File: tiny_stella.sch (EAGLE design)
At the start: 73 parts, among them SW1 RGT_DIFFICULTY, SW2 LFT_DIFFICULTY, SW3 ON/OFF, T1 2N3904, T2 PN3906, T3 PN3906, X1 SSW-112-02-G-Q

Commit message: labeled everything and started laying traces
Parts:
- S3, S4: device SparkFun-Switches:MOMENTARY-SWITCH-SPST-SMD-6.0X3.5MM -> SparkFun-Switches:MOMENTARY-SWITCH-SPST-PTH-6.0MM-KIT
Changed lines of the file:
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@@
 <part name="GND14" library="supply1" library_urn="urn:adsk.eagle:library:371" deviceset="GND" device=""/>
 <part name="GND15" library="supply1" library_urn="urn:adsk.eagle:library:371" deviceset="GND" device=""/>
-<part name="S3" library="SparkFun-Switches" library_urn="urn:adsk.eagle:library:535" deviceset="MOMENTARY-SWITCH-SPST" device="-SMD-6.0X3.5MM" package3d_urn="urn:adsk.eagle:package:40165/1" value="START"/>
-<part name="S4" library="SparkFun-Switches" library_urn="urn:adsk.eagle:library:535" deviceset="MOMENTARY-SWITCH-SPST" device="-SMD-6.0X3.5MM" package3d_urn="urn:adsk.eagle:package:40165/1" value="SELECT"/>
+<part name="S3" library="SparkFun-Switches" library_urn="urn:adsk.eagle:library:535" deviceset="MOMENTARY-SWITCH-SPST" device="-PTH-6.0MM-KIT" package3d_urn="urn:adsk.eagle:package:40170/1" value="START"/>
+<part name="S4" library="SparkFun-Switches" library_urn="urn:adsk.eagle:library:535" deviceset="MOMENTARY-SWITCH-SPST" device="-PTH-6.0MM-KIT" package3d_urn="urn:adsk.eagle:package:40170/1" value="SELECT"/>
 <part name="C10" library="resistor" library_urn="urn:adsk.eagle:library:348" deviceset="C-US" device="C0805" package3d_urn="urn:adsk.eagle:package:26137/1" value="10nF"/>
 <part name="GND16" library="supply1" library_urn="urn:adsk.eagle:library:371" deviceset="GND" device=""/>

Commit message: added pausing circuitry
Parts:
- added C21: 100nF, resistor:C-USC0805
- added D1, D2, D3: (no value), eagle-ltspice:DIODE_E-
- added IC1: 74LS00D, 74xx-us:74LS00D
- added R32: 1.5k, resistor:R-US_M0805
- added R33, R34: 1k, resistor:R-US_M0805
- added SW4: ON/OFF, special:SW_DIP-1
- added T4: PN3906, User-Submitted:TRANSISTOR_PNPPMBT3906
- R17: value 4.7k -> 1k
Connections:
- removed net RDY: R17.1, U$1.!RDY, U$2.RDY
- new net CPU_RDY: IC1D.O, U$2.RDY
- new net N$34: R17.1, T4.C
- new net N$35: IC1B.I1, IC1C.O, IC1D.I0, IC1D.I1
- new net N$36: D3.C, IC1A.I1
- new net N$38: IC1A.O, IC1B.I0
- new net N$39: D1.C, IC1B.O, IC1C.I1
- new net N$40: D1.A, D2.A, IC1A.I0, IC1C.I0, R33.1
- new net P_SW: D3.A, R34.2, SW4.2, T4.B
- new net TIA_RDY: D2.C, R32.2, U$1.!RDY
- net +5V: now also R32.1, R34.1; no longer R17.2
- net GND: now also C21.2, R17.2, R33.2, SW4.1
- net N$13: now also T4.E
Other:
- moved on the sheet: C12, C13, R17, SW3, USB1

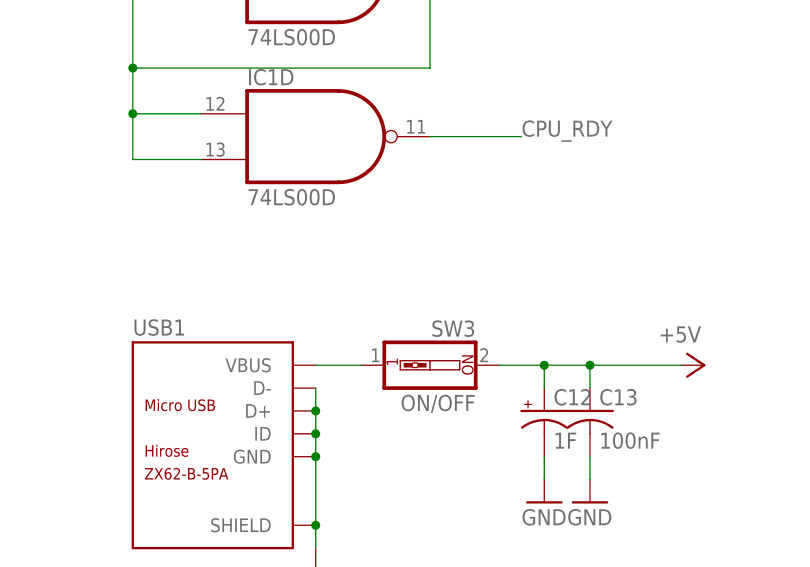
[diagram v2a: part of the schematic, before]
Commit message: added breakout for the power
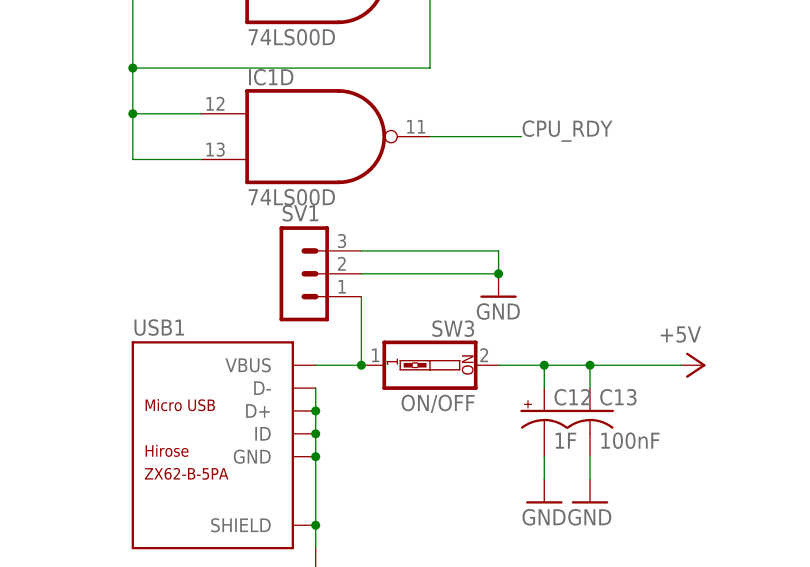
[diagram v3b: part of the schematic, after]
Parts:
- added SV1: (no value), con-lstb:MA03-1
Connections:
- net GND: now also SV1.2, SV1.3
- net VBUS: now also SV1.1
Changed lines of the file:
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@@
 <part name="GND38" library="supply1" library_urn="urn:adsk.eagle:library:371" deviceset="GND" device=""/>
 <part name="T4" library="User-Submitted" library_urn="urn:adsk.eagle:library:536" deviceset="TRANSISTOR_PNP" device="PMBT3906" package3d_urn="urn:adsk.eagle:package:40256/1" value="PN3906"/>
+<part name="SV1" library="con-lstb" library_urn="urn:adsk.eagle:library:162" deviceset="MA03-1" device="" package3d_urn="urn:adsk.eagle:package:8339/1"/>
+<part name="GND39" library="supply1" library_urn="urn:adsk.eagle:library:371" deviceset="GND" device=""/>
 </parts>
 <sheets>
@@
 <instance part="GND38" gate="1" x="264.16" y="33.02" rot="MR0"/>
 <instance part="T4" gate="G$1" x="261.62" y="55.88"/>
+<instance part="SV1" gate="G$1" x="-119.38" y="55.88"/>
+<instance part="GND39" gate="1" x="-96.52" y="53.34"/>
 </instances>
 <busses>
@@
 <pinref part="GND38" gate="1" pin="GND"/>
 </segment>
+<segment>
+<pinref part="SV1" gate="G$1" pin="2"/>
+<wire x1="-111.76" y1="55.88" x2="-96.52" y2="55.88" width="0.1524" layer="91"/>
+<pinref part="SV1" gate="G$1" pin="3"/>
+<wire x1="-96.52" y1="55.88" x2="-96.52" y2="58.42" width="0.1524" layer="91"/>
+<wire x1="-96.52" y1="58.42" x2="-111.76" y2="58.42" width="0.1524" layer="91"/>
+<pinref part="GND39" gate="1" pin="GND"/>
+<junction x="-96.52" y="55.88"/>
+</segment>
 </net>
 <net name="N$9" class="0">
@@
 <pinref part="SW3" gate="G$1" pin="1"/>
 <wire x1="-116.84" y1="45.72" x2="-111.76" y2="45.72" width="0.1524" layer="91"/>
-</segment>
-</net>
+<pinref part="SV1" gate="G$1" pin="1"/>
+<wire x1="-111.76" y1="45.72" x2="-111.76" y2="53.34" width="0.1524" layer="91"/>
+<junction x="-111.76" y="45.72"/>
+</segment>
+</net>

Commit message: silkscreen work
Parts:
- renumbered U$1 to TIA, U$2 to 6507, U$3 to 6532

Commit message: yet more silkscreen
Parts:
- renumbered BRT_ADJ to BRIGHTNESS, SW1 to RDIFF, SW2 to LDIFF, SW3 to ON/OFF, SW4 to PAUSE
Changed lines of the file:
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@@
 <part name="GND16" library="supply1" library_urn="urn:adsk.eagle:library:371" deviceset="GND" device=""/>
 <part name="JP1" library="SparkFun-Jumpers" library_urn="urn:adsk.eagle:library:528" deviceset="JUMPER-SMT_2_NO" device="_NO-SILK" package3d_urn="urn:adsk.eagle:package:39277/1" value="COLOR/BW"/>
-<part name="SW1" library="special" library_urn="urn:adsk.eagle:library:367" deviceset="SW_DIP-1" device="" package3d_urn="urn:adsk.eagle:package:26661/1" value="RGT_DIFFICULTY"/>
-<part name="SW2" library="special" library_urn="urn:adsk.eagle:library:367" deviceset="SW_DIP-1" device="" package3d_urn="urn:adsk.eagle:package:26661/1" value="LFT_DIFFICULTY"/>
+<part name="RDIFF" library="special" library_urn="urn:adsk.eagle:library:367" deviceset="SW_DIP-1" device="" package3d_urn="urn:adsk.eagle:package:26661/1" value="RGT_DIFFICULTY"/>
+<part name="LDIFF" library="special" library_urn="urn:adsk.eagle:library:367" deviceset="SW_DIP-1" device="" package3d_urn="urn:adsk.eagle:package:26661/1" value="LFT_DIFFICULTY"/>
 <part name="GND17" library="supply1" library_urn="urn:adsk.eagle:library:371" deviceset="GND" device=""/>
 <part name="JP2" library="SparkFun-Jumpers" library_urn="urn:adsk.eagle:library:528" deviceset="JUMPER-SMT_2_NO" device="_NO-SILK" package3d_urn="urn:adsk.eagle:package:39277/1" value="CPU_RES"/>
@@
 <part name="T1" library="transistor" library_urn="urn:adsk.eagle:library:402" deviceset="*-NPN-" device="SOT23-BEC" package3d_urn="urn:adsk.eagle:package:29919/2" technology="MMBT3904LT1" value="2N3904"/>
 <part name="T2" library="User-Submitted" library_urn="urn:adsk.eagle:library:536" deviceset="TRANSISTOR_PNP" device="PMBT3906" package3d_urn="urn:adsk.eagle:package:40256/1" value="PN3906"/>
-<part name="BRT_ADJ" library="pot" library_urn="urn:adsk.eagle:library:331" deviceset="TRIM_US-" device="3223G" package3d_urn="urn:adsk.eagle:package:22722/1" value="500k"/>
+<part name="BRIGHTNESS" library="pot" library_urn="urn:adsk.eagle:library:331" deviceset="TRIM_US-" device="3223G" package3d_urn="urn:adsk.eagle:package:22722/1" value="500k"/>
 <part name="R19" library="resistor" library_urn="urn:adsk.eagle:library:348" deviceset="R-US_" device="M0805" package3d_urn="urn:adsk.eagle:package:26079/1" value="1k"/>
 <part name="R20" library="resistor" library_urn="urn:adsk.eagle:library:348" deviceset="R-US_" device="M0805" package3d_urn="urn:adsk.eagle:package:26079/1" value="3.3k"/>
@@
 <part name="GND29" library="supply1" library_urn="urn:adsk.eagle:library:371" deviceset="GND" device=""/>
 <part name="GND30" library="supply1" library_urn="urn:adsk.eagle:library:371" deviceset="GND" device=""/>
-<part name="SW3" library="special" library_urn="urn:adsk.eagle:library:367" deviceset="SW_DIP-1" device="" package3d_urn="urn:adsk.eagle:package:26661/1" value="ON/OFF"/>
+<part name="ON/OFF" library="special" library_urn="urn:adsk.eagle:library:367" deviceset="SW_DIP-1" device="" package3d_urn="urn:adsk.eagle:package:26661/1" value="ON/OFF"/>
 <part name="P+24" library="supply1" library_urn="urn:adsk.eagle:library:371" deviceset="+5V" device=""/>
 <part name="R27" library="resistor" library_urn="urn:adsk.eagle:library:348" deviceset="R-US_" device="M0805" package3d_urn="urn:adsk.eagle:package:26079/1" value="24k"/>
@@
 <part name="R33" library="resistor" library_urn="urn:adsk.eagle:library:348" deviceset="R-US_" device="M0805" package3d_urn="urn:adsk.eagle:package:26079/1" value="1k"/>
 <part name="R34" library="resistor" library_urn="urn:adsk.eagle:library:348" deviceset="R-US_" device="M0805" package3d_urn="urn:adsk.eagle:package:26079/1" value="1k"/>
-<part name="SW4" library="special" library_urn="urn:adsk.eagle:library:367" deviceset="SW_DIP-1" device="" package3d_urn="urn:adsk.eagle:package:26661/1" value="ON/OFF"/>
+<part name="PAUSE" library="special" library_urn="urn:adsk.eagle:library:367" deviceset="SW_DIP-1" device="" package3d_urn="urn:adsk.eagle:package:26661/1" value="ON/OFF"/>
 <part name="D3" library="eagle-ltspice" library_urn="urn:adsk.eagle:library:217" deviceset="DIODE_E-" device="" package3d_urn="urn:adsk.eagle:package:13312/1"/>
 <part name="C21" library="resistor" library_urn="urn:adsk.eagle:library:348" deviceset="C-US" device="C0805" package3d_urn="urn:adsk.eagle:package:26137/1" value="100nF"/>
@@
 <instance part="GND16" gate="1" x="83.82" y="91.44"/>
 <instance part="JP1" gate="G$1" x="71.12" y="86.36"/>
-<instance part="SW1" gate="G$1" x="78.74" y="63.5" rot="MR180"/>
-<instance part="SW2" gate="G$1" x="78.74" y="76.2" rot="MR180"/>
+<instance part="RDIFF" gate="G$1" x="78.74" y="63.5" rot="MR180"/>
+<instance part="LDIFF" gate="G$1" x="78.74" y="76.2" rot="MR180"/>
 <instance part="GND17" gate="1" x="93.98" y="55.88"/>
 <instance part="JP2" gate="G$1" x="10.16" y="-2.54"/>
@@
 <instance part="T1" gate="G$1" x="287.02" y="68.58"/>
 <instance part="T2" gate="G$1" x="299.72" y="68.58"/>
-<instance part="BRT_ADJ" gate="G$1" x="269.24" y="68.58" rot="MR0"/>
+<instance part="BRIGHTNESS" gate="G$1" x="269.24" y="68.58" rot="MR0"/>
 <instance part="R19" gate="G$1" x="254" y="68.58" rot="MR0"/>
 <instance part="R20" gate="G$1" x="279.4" y="83.82" rot="MR270"/>
@@
 <instance part="GND29" gate="1" x="-20.32" y="60.96"/>
 <instance part="GND30" gate="1" x="144.78" y="93.98" rot="MR0"/>
-<instance part="SW3" gate="G$1" x="-104.14" y="45.72" rot="MR0"/>
+<instance part="ON/OFF" gate="G$1" x="-104.14" y="45.72" rot="MR0"/>
 <instance part="P+24" gate="1" x="177.8" y="-22.86" rot="MR90"/>
 <instance part="R27" gate="G$1" x="66.04" y="-22.86" rot="MR0"/>
@@
 <instance part="R33" gate="G$1" x="-88.9" y="124.46" rot="MR270"/>
 <instance part="R34" gate="G$1" x="-162.56" y="142.24" rot="MR270"/>
-<instance part="SW4" gate="G$1" x="-185.42" y="137.16" rot="MR0"/>
+<instance part="PAUSE" gate="G$1" x="-185.42" y="137.16" rot="MR0"/>
 <instance part="D3" gate="G$1" x="-149.86" y="137.16" rot="R270"/>
 <instance part="C21" gate="G$1" x="-147.32" y="129.54"/>
@@
 <wire x1="-86.36" y1="43.18" x2="-86.36" y2="45.72" width="0.1524" layer="91"/>
 <junction x="-86.36" y="45.72"/>
-<pinref part="SW3" gate="G$1" pin="2"/>
+<pinref part="ON/OFF" gate="G$1" pin="2"/>
 <wire x1="-96.52" y1="45.72" x2="-91.44" y2="45.72" width="0.1524" layer="91"/>
 <junction x="-91.44" y="45.72"/>
@@
 <pinref part="JP1" gate="G$1" pin="2"/>
 <wire x1="76.2" y1="86.36" x2="93.98" y2="86.36" width="0.1524" layer="91"/>
-<pinref part="SW2" gate="G$1" pin="1"/>
+<pinref part="LDIFF" gate="G$1" pin="1"/>
 <wire x1="86.36" y1="76.2" x2="93.98" y2="76.2" width="0.1524" layer="91"/>
 <wire x1="93.98" y1="86.36" x2="93.98" y2="76.2" width="0.1524" layer="91"/>
-<pinref part="SW1" gate="G$1" pin="1"/>
+<pinref part="RDIFF" gate="G$1" pin="1"/>
 <wire x1="86.36" y1="63.5" x2="93.98" y2="63.5" width="0.1524" layer="91"/>
 <wire x1="93.98" y1="76.2" x2="93.98" y2="63.5" width="0.1524" layer="91"/>
@@
 </segment>
 <segment>
-<pinref part="SW4" gate="G$1" pin="1"/>
+<pinref part="PAUSE" gate="G$1" pin="1"/>
 <pinref part="GND35" gate="1" pin="GND"/>
 <wire x1="-193.04" y1="137.16" x2="-198.12" y2="137.16" width="0.1524" layer="91"/>
@@
 <wire x1="58.42" y1="53.34" x2="68.58" y2="53.34" width="0.1524" layer="91"/>
 <wire x1="68.58" y1="53.34" x2="68.58" y2="60.96" width="0.1524" layer="91"/>
-<pinref part="SW2" gate="G$1" pin="2"/>
+<pinref part="LDIFF" gate="G$1" pin="2"/>
 <wire x1="71.12" y1="76.2" x2="68.58" y2="76.2" width="0.1524" layer="91"/>
 <wire x1="68.58" y1="76.2" x2="68.58" y2="60.96" width="0.1524" layer="91"/>
@@
 <net name="N$22" class="0">
 <segment>
-<pinref part="SW1" gate="G$1" pin="2"/>
+<pinref part="RDIFF" gate="G$1" pin="2"/>
 <wire x1="71.12" y1="63.5" x2="71.12" y2="48.26" width="0.1524" layer="91"/>
 <pinref part="6532" gate="G$1" pin="PB7"/>
@@
 <pinref part="R21" gate="G$1" pin="1"/>
 <wire x1="279.4" y1="68.58" x2="279.4" y2="60.96" width="0.1524" layer="91"/>
-<pinref part="BRT_ADJ" gate="G$1" pin="A"/>
+<pinref part="BRIGHTNESS" gate="G$1" pin="A"/>
 <wire x1="269.24" y1="60.96" x2="274.32" y2="60.96" width="0.1524" layer="91"/>
 <wire x1="274.32" y1="60.96" x2="274.32" y2="68.58" width="0.1524" layer="91"/>
@@
 <segment>
 <pinref part="R19" gate="G$1" pin="1"/>
-<pinref part="BRT_ADJ" gate="G$1" pin="S"/>
+<pinref part="BRIGHTNESS" gate="G$1" pin="S"/>
 <wire x1="259.08" y1="68.58" x2="264.16" y2="68.58" width="0.1524" layer="91"/>
 <wire x1="264.16" y1="60.96" x2="264.16" y2="68.58" width="0.1524" layer="91"/>
@@
 <segment>
 <pinref part="USB1" gate="G$1" pin="VBUS"/>
-<pinref part="SW3" gate="G$1" pin="1"/>
+<pinref part="ON/OFF" gate="G$1" pin="1"/>
 <wire x1="-116.84" y1="45.72" x2="-111.76" y2="45.72" width="0.1524" layer="91"/>
 <pinref part="SV1" gate="G$1" pin="1"/>
@@
 <segment>
 <pinref part="R34" gate="G$1" pin="2"/>
-<pinref part="SW4" gate="G$1" pin="2"/>
+<pinref part="PAUSE" gate="G$1" pin="2"/>
 <wire x1="-162.56" y1="137.16" x2="-177.8" y2="137.16" width="0.1524" layer="91"/>
 <label x="-170.18" y="137.16" size="1.778" layer="95" rot="R180"/>
